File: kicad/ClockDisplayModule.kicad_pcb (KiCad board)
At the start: 2 copper layers, 88.9 x 33 mm, 13 parts, among them P101 CONN_01X05, U101 MAX7221

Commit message: Initial layout before routing
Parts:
- AFF101, AFF102, AFF103, AFF104: value 7SEGMENTS-CC -> NKR161B; footprint ClockFootprints:SC08-11SURKWA -> ClockFootprints:161_163_Series
- U101: footprint SMD_Packages:SOIC-24 -> ClockFootprints:SOIC-24
- moved R101 24.2 mm to (117.9, 39.9), turned to 90 degrees
- moved C101 12.0 mm to (113.8, 40.4), turned to 270 degrees
- moved D104 12.0 mm to (145.8, 41.9)
- moved D103 11.7 mm to (146.1, 61.0)
- moved AFF104 10.9 mm to (93.5, 52.1)
- moved C102 10.9 mm to (115.1, 45.5), turned to 0 degrees
- moved U101 10.4 mm to (115.3, 52.3), turned to 0 degrees
- moved AFF101 9.40 mm to (136.7, 52.1)
- moved P101 9.15 mm to (110.2, 67.1)
- moved AFF103 3.56 mm to (106.4, 52.1)
- moved D101 2.18 mm to (115.6, 47.5)
- moved AFF102 2.03 mm to (123.7, 52.1)
- moved D102 1.63 mm to (115.6, 54.4)
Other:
- net class Default: clearance 0.2 -> 0.254; trace_width 0.25 -> 0.254; via_dia 0.6 -> 0.6858; via_drill 0.4 -> 0.3302
- rule trace_clearance: 0.2 -> 0.254
- rule trace_min: 0.2 -> 0.1524
- rule via_min_drill: 0.3 -> 0.3302
- rule via_min_size: 0.4 -> 0.6858

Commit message: Layout complete and board ordered
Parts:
- added G***: LOGO, ClockFootprints:kicad_logo, F.Cu at (78.7, 65.0)
- added G***: LOGO, ClockFootprints:osh_outline_logo, F.Cu at (77.2, 41.4)
- added R102: 0, Resistors_SMD:R_0805_HandSoldering, F.Cu at (110.0, 47.8)
- added R103: 0, Resistors_SMD:R_0805_HandSoldering, F.Cu at (120.1, 54.6)
- added R104: 0, Resistors_SMD:R_0805_HandSoldering, B.Cu at (150.1, 62.0)
- added R105: 0, Resistors_SMD:R_0805_HandSoldering, B.Cu at (147.3, 38.1)
- moved P101 47.3 mm to (157.5, 66.0), turned to 270 degrees
- moved U101 34.3 mm to (149.6, 52.6), turned to 90 degrees
- moved C102 28.7 mm to (142.2, 54.6), turned to 270 degrees
- moved C101 26.1 mm to (136.4, 53.3), turned to 0 degrees
- moved R101 24.0 mm to (140.0, 49.3), turned to 0 degrees
- moved D101 1.27 mm to (115.6, 48.8)
- moved D102 0.76 mm to (115.6, 53.6), turned to 270 degrees
- turned D103 to 270 degrees
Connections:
- AFF101 pad 5: Net-(AFF101-Pad5) -> (no net)
- AFF102 pad 5: Net-(AFF102-Pad5) -> (no net)
- AFF103 pad 5: Net-(AFF103-Pad5) -> (no net)
- AFF104 pad 5: Net-(AFF104-Pad5) -> (no net)
- D101 pad 1: Signal -> Colon
- D101 pad 2: Seg_A -> Net-(D101-Pad2)
- D102 pad 1: Signal -> Colon
- D102 pad 2: Seg_B -> Net-(D102-Pad2)
- D103 pad 2: Seg_C -> Net-(D103-Pad2)
- D104 pad 2: Seg_D -> Net-(D104-Pad2)
- U101 pad 10: Net-(U101-Pad10) -> Signal
- U101 pad 22: Net-(U101-Pad22) -> (no net)
- U101 pad 24: Net-(U101-Pad24) -> (no net)
- U101 pad 3: Signal -> Colon
- U101 pad 5: Net-(U101-Pad5) -> (no net)
- U101 pad 8: Net-(U101-Pad8) -> (no net)
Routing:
- net Seg_A: track 0.00 -> 112.7 mm, vias 0 -> 7
- net Seg_B: track 0.00 -> 99.9 mm, vias 0 -> 2
- net Seg_G: track 0.00 -> 92.6 mm, vias 0 -> 6
- net Dig_3: track 0.00 -> 91.0 mm, vias 0 -> 1
- net Seg_F: track 0.00 -> 84.0 mm, vias 0 -> 6
- net Dig_2: track 0.00 -> 78.9 mm, vias 0 -> 1
- net Seg_E: track 0.00 -> 74.3 mm, vias 0 -> 4
- net Dig_0: track 0.00 -> 70.5 mm, vias 0 -> 3
- net Seg_C: track 0.00 -> 67.5 mm, vias 0 -> 1
- net Seg_D: track 0.00 -> 64.1 mm, vias 0 -> 4
- net Dig_1: track 0.00 -> 60.7 mm, vias 0 -> 1
- net Colon: track 0.00 -> 59.2 mm, vias 0 -> 1
- net Signal: track 0.00 -> 27.9 mm, vias 0 -> 1
- net CLK: track 0.00 -> 25.1 mm, vias 0 -> 2
- net ~SS: track 0.00 -> 24.5 mm, vias 0 -> 1
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- added copper zone on GND, net GND
- added copper zone on V+, net V+
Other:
- copper layers 2 -> 4
- board text added: "+"
- board text added: "CLK"
- board text added: "Clock Display Module Rev 4L.2"
- board text added: "G"
- board text added: "MOSI"
- board text added: "~SS"

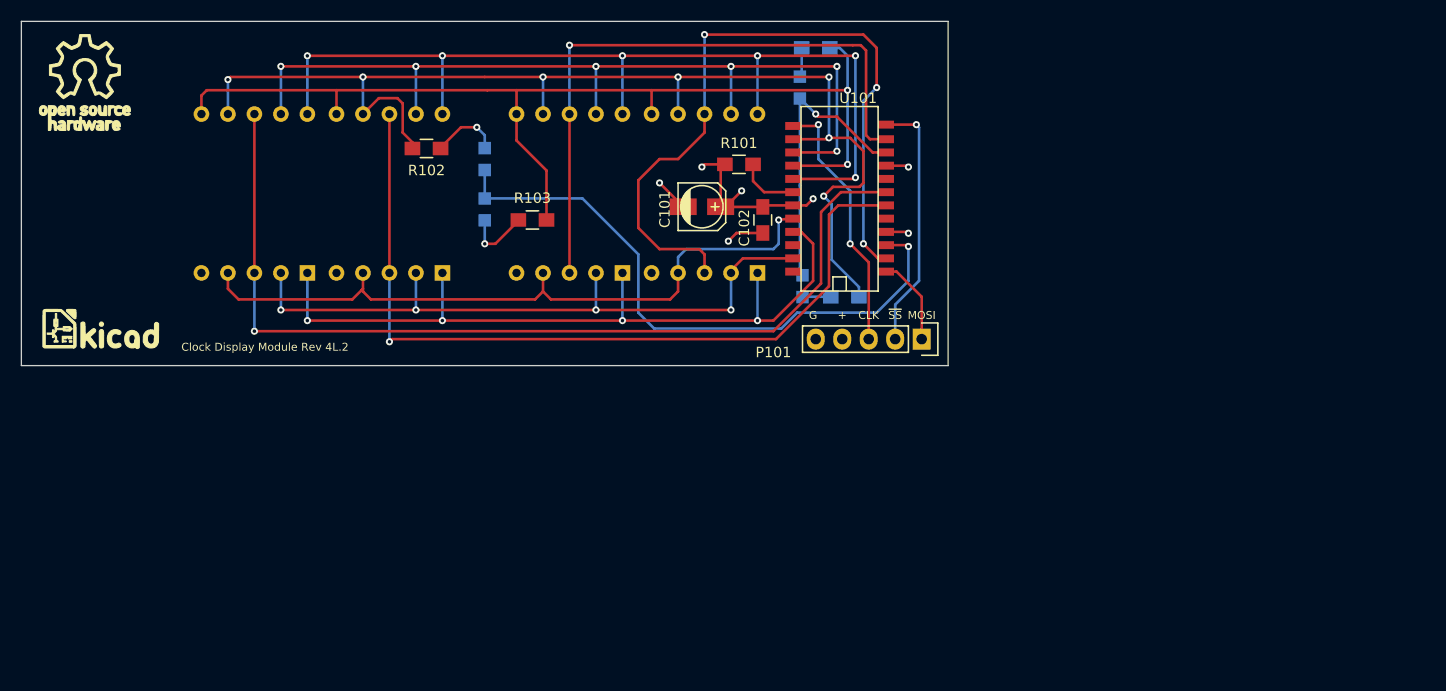
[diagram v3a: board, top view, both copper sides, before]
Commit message: Started layout
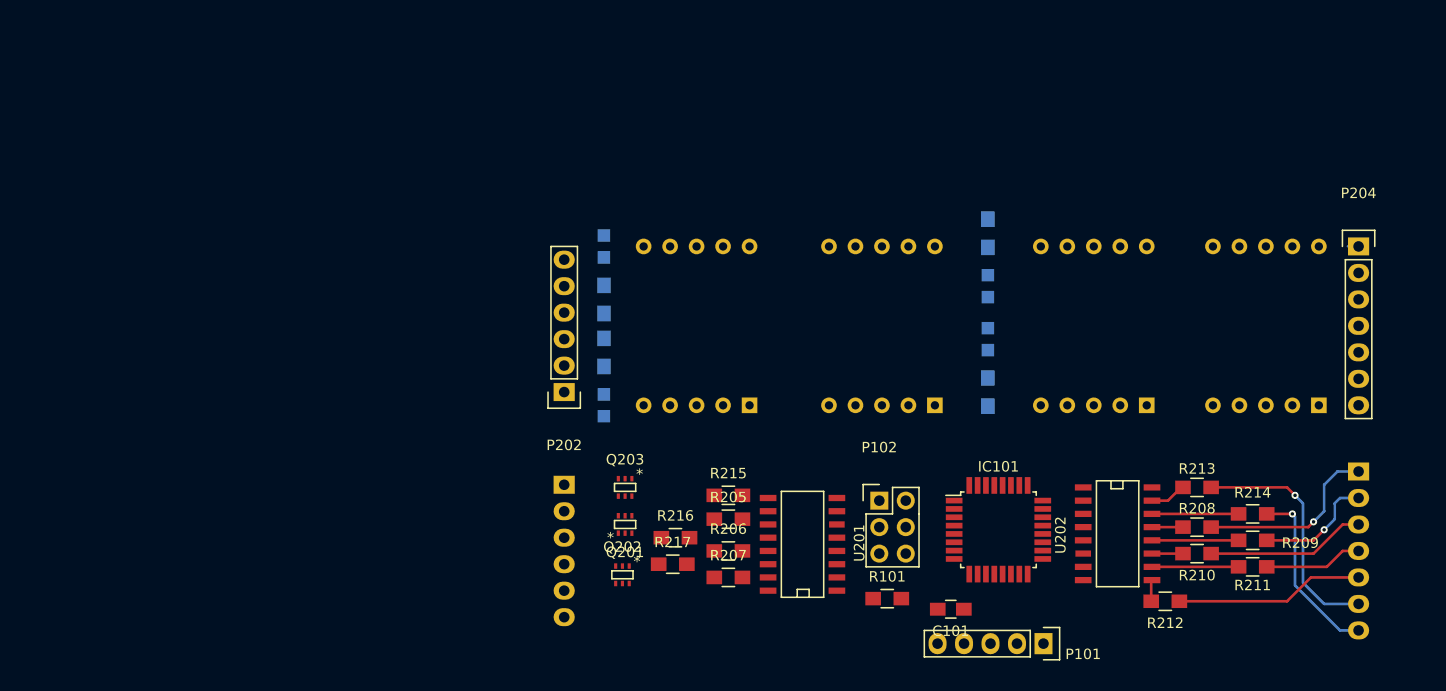
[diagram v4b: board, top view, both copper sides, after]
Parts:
- removed AFF101, AFF102, AFF103, AFF104: NKR161B, ClockFootprints:161_163_Series
- removed C102: 0.1u, Capacitors_SMD:C_0805_HandSoldering
- removed D101: Colon1, LEDs:LED-0805
- removed D102: Colon2, LEDs:LED-0805
- removed D103: Alarm, LEDs:LED-0805
- removed D104: Auto, LEDs:LED-0805
- removed G***: LOGO, ClockFootprints:kicad_logo
- removed G***: LOGO, ClockFootprints:osh_outline_logo
- removed R102, R103, R104, R105: 0, Resistors_SMD:R_0805_HandSoldering
- removed U101: MAX7221, ClockFootprints:SOIC-24
- added AFF201: NKR161B, ClockFootprints:161_163_Series, B.Cu at (135.9, 64.8)
- added AFF202: NKR161B, ClockFootprints:161_163_Series, B.Cu at (174.0, 64.8)
- added AFF203: NKR161B, ClockFootprints:161_163_Series, B.Cu at (153.7, 64.8)
- added AFF204: NKR161B, ClockFootprints:161_163_Series, B.Cu at (190.5, 64.8)
- added D201: Colon1, LEDs:LED-0805, B.Cu at (163.8, 66.0)
- added D202: Colon2, LEDs:LED-0805, B.Cu at (163.8, 61.0)
- added D203: Alarm, LEDs:LED-0805, B.Cu at (127.0, 57.1)
- added D204: Auto, LEDs:LED-0805, B.Cu at (127.0, 72.4)
- added IC101: ATMEGA8-P, Housings_QFP:TQFP-32_7x7mm_Pitch0.8mm, F.Cu at (164.8, 84.3)
- added P102: CONN_02X03, Pin_Headers:Pin_Header_Straight_2x03, F.Cu at (153.4, 81.5)
- added P201: CONN_01X07, Pin_Headers:Pin_Header_Straight_1x07, B.Cu at (199.4, 78.7)
- added P202: CONN_01X06, Pin_Headers:Pin_Header_Straight_1x06, F.Cu at (123.2, 71.1)
- added P203: CONN_01X06, Pin_Headers:Pin_Header_Straight_1x06, B.Cu at (123.2, 80.0)
- added P204: CONN_01X07, Pin_Headers:Pin_Header_Straight_1x07, F.Cu at (199.4, 57.1)
- added Q201: BC856BS, ClockFootprints:SOT-363, F.Cu at (129.0, 83.8)
- added Q202: BC856BS, ClockFootprints:SOT-363, F.Cu at (128.8, 88.6)
- added Q203: BC856BS, ClockFootprints:SOT-363, F.Cu at (129.0, 80.3)
- added R201: 0, Resistors_SMD:R_0805_HandSoldering, B.Cu at (163.8, 71.1)
- added R202: 0, Resistors_SMD:R_0805_HandSoldering, B.Cu at (163.8, 55.9)
- added R203: 0, Resistors_SMD:R_0805_HandSoldering, B.Cu at (127.0, 62.2)
- added R204: 0, Resistors_SMD:R_0805_HandSoldering, B.Cu at (127.0, 67.3)
- added R205: 500, Resistors_SMD:R_0805_HandSoldering, F.Cu at (138.9, 83.3)
- added R206: 500, Resistors_SMD:R_0805_HandSoldering, F.Cu at (138.9, 86.4)
- added R207: 500, Resistors_SMD:R_0805_HandSoldering, F.Cu at (138.9, 88.9)
- added R208: 160, Resistors_SMD:R_0805_HandSoldering, F.Cu at (183.9, 84.1)
- added R209: 160, Resistors_SMD:R_0805_HandSoldering, F.Cu at (189.2, 85.3)
- added R210: 160, Resistors_SMD:R_0805_HandSoldering, F.Cu at (183.9, 86.6)
- added R211: 160, Resistors_SMD:R_0805_HandSoldering, F.Cu at (189.2, 87.9)
- added R212: 160, Resistors_SMD:R_0805_HandSoldering, F.Cu at (180.8, 91.2)
- added R213: 160, Resistors_SMD:R_0805_HandSoldering, F.Cu at (183.9, 80.3)
- added R214: 160, Resistors_SMD:R_0805_HandSoldering, F.Cu at (189.2, 82.8)
- added R215: 500, Resistors_SMD:R_0805_HandSoldering, F.Cu at (138.9, 81.0)
- added R216: 500, Resistors_SMD:R_0805_HandSoldering, F.Cu at (133.9, 85.1)
- added R217: 500, Resistors_SMD:R_0805_HandSoldering, F.Cu at (133.6, 87.6)
- added U201: SN74LS138, ClockFootprints:SOIC-16, F.Cu at (146.1, 85.6)
- added U202: 74HC4511, ClockFootprints:SOIC-16, F.Cu at (176.3, 84.8)
- C101: value 10u -> 0.1u; footprint Capacitors_SMD:c_elec_4x5.8 -> Capacitors_SMD:C_0805_HandSoldering
- R101: value 25K -> 10K
- moved C101 45.4 mm to (160.3, 91.9), turned to 180 degrees
- moved R101 44.0 mm to (154.2, 90.9)
- moved P101 31.5 mm to (169.2, 95.2)
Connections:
- net V+ renamed VCC
- R101 pad 2: Net-(R101-Pad2) -> Reset
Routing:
- net Seg_A: track 112.7 -> 0.00 mm, vias 7 -> 0
- net Seg_B: track 99.9 -> 0.00 mm, vias 2 -> 0
- net Seg_G: track 92.6 -> 0.00 mm, vias 6 -> 0
- net Dig_3: track 91.0 -> 0.00 mm, vias 1 -> 0
- net Seg_F: track 84.0 -> 0.00 mm, vias 6 -> 0
- net Dig_2: track 78.9 -> 0.00 mm, vias 1 -> 0
- net Seg_E: track 74.3 -> 0.00 mm, vias 4 -> 0
- net Dig_0: track 70.5 -> 0.00 mm, vias 3 -> 0
- net Seg_C: track 67.5 -> 0.00 mm, vias 1 -> 0
- net Seg_D: track 64.1 -> 0.00 mm, vias 4 -> 0
- net Dig_1: track 60.7 -> 0.00 mm, vias 1 -> 0
- net Colon: track 59.2 -> 0.00 mm, vias 1 -> 0
- net Signal: track 27.9 -> 0.00 mm, vias 1 -> 0
- net CLK: track 25.1 -> 0.00 mm, vias 2 -> 0
- net ~SS: track 24.5 -> 0.00 mm, vias 1 -> 0
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- removed copper zone on GND, net GND
- removed copper zone on V+, net VCC
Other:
- board outline removed
- copper layers 4 -> 2
- board text removed: "+"
- board text removed: "CLK"
- board text removed: "Clock Display Module Rev 4L.2"
- board text removed: "G"
- board text removed: "MOSI"
- board text removed: "~SS"

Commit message: Updated the layout for the controller side
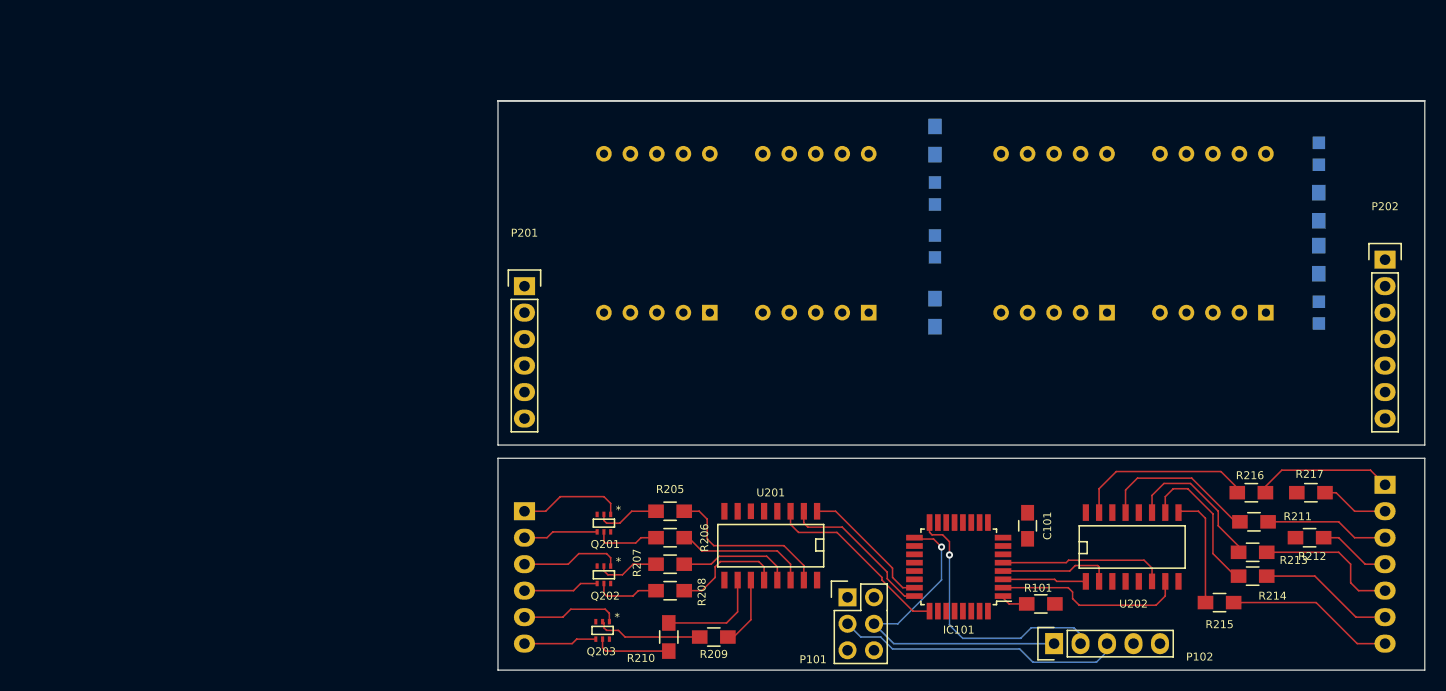
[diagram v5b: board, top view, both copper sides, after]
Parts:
- P101: value CONN_01X05 -> CONN_02X03; footprint Pin_Headers:Pin_Header_Straight_1x05 -> Pin_Headers:Pin_Header_Straight_2x03
- P102: value CONN_02X03 -> CONN_01X05; footprint Pin_Headers:Pin_Header_Straight_2x03 -> Pin_Headers:Pin_Header_Straight_1x05
- P201: value CONN_01X07 -> CONN_01X06; footprint Pin_Headers:Pin_Header_Straight_1x07 -> Pin_Headers:Pin_Header_Straight_1x06; moved to F.Cu
- P202: value CONN_01X06 -> CONN_01X07; footprint Pin_Headers:Pin_Header_Straight_1x06 -> Pin_Headers:Pin_Header_Straight_1x07
- P204: moved to B.Cu
- R208, R209, R210: value 160 -> 500
- R215, R216, R217: value 500 -> 160
- moved P201 82.0 mm to (119.4, 61.0), turned to 0 degrees
- moved P202 79.8 mm to (201.9, 58.4), turned to 0 degrees
- moved D203 69.2 mm to (195.6, 48.3)
- moved D204 69.2 mm to (195.6, 63.5)
- moved R203 69.2 mm to (195.6, 53.3)
- moved R204 69.2 mm to (195.6, 58.4)
- moved R217 61.6 mm to (194.8, 80.8), turned to 180 degrees
- moved AFF204 59.1 mm to (132.1, 55.9)
- moved R216 55.4 mm to (189.1, 80.8), turned to 180 degrees
- moved R209 52.5 mm to (137.5, 94.6), turned to 0 degrees
- moved R210 51.3 mm to (133.2, 94.6), turned to 90 degrees
- moved R208 50.9 mm to (133.3, 90.2), turned to 0 degrees
- moved AFF201 50.3 mm to (185.4, 55.9)
- moved R215 48.2 mm to (186.1, 91.3), turned to 180 degrees
- moved P204 23.0 mm to (201.9, 80.0), turned to 180 degrees
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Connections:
- AFF201 pad 5: Net-(AFF201-Pad5) -> (no net)
- AFF202 pad 5: Net-(AFF202-Pad5) -> (no net)
- AFF203 pad 5: Net-(AFF203-Pad5) -> (no net)
- AFF204 pad 5: Net-(AFF204-Pad5) -> (no net)
- IC101 pad 10: Net-(IC101-Pad10) -> (no net)
- IC101 pad 11: Net-(IC101-Pad11) -> (no net)
- IC101 pad 12: Net-(IC101-Pad12) -> (no net)
- IC101 pad 13: Net-(IC101-Pad13) -> (no net)
- IC101 pad 14: Net-(IC101-Pad14) -> (no net)
- IC101 pad 15: Net-(IC101-Pad15) -> (no net)
- IC101 pad 18: Net-(IC101-Pad18) -> MISO
- IC101 pad 21: Net-(IC101-Pad21) -> (no net)
- IC101 pad 26: Net-(IC101-Pad26) -> (no net)
- IC101 pad 27: Net-(IC101-Pad27) -> (no net)
- IC101 pad 28: Net-(IC101-Pad28) -> (no net)
- IC101 pad 6: Net-(IC101-Pad6) -> (no net)
- IC101 pad 9: Net-(IC101-Pad9) -> (no net)
- P101 pad 1: MOSI -> MISO
- P101 pad 2: ~SS -> VCC
- P101 pad 4: VCC -> MOSI
- P101 pad 5: GND -> Reset
- P102 pad 2: VCC -> ~SS
- P102 pad 4: MOSI -> VCC
- P102 pad 5: Reset -> GND
- P201 pad 1: Net-(P201-Pad1) -> D_Dig_0
- P201 pad 2: Net-(P201-Pad2) -> D_Dig_1
- P201 pad 3: Net-(P201-Pad3) -> D_Dig_2
- P201 pad 4: Net-(P201-Pad4) -> D_Dig_3
- P201 pad 5: Net-(P201-Pad5) -> D_Colon
- P201 pad 6: Net-(P201-Pad6) -> D_Signal
- P202 pad 1: D_Dig_0 -> /Display Driver/Seg_A
- P202 pad 2: D_Dig_1 -> /Display Driver/Seg_B
- P202 pad 3: D_Dig_2 -> /Display Driver/Seg_C
- P202 pad 4: D_Dig_3 -> /Display Driver/Seg_D
- P202 pad 5: D_Colon -> /Display Driver/Seg_E
- P202 pad 6: D_Signal -> /Display Driver/Seg_F
- P204 pad 1: /Display Driver/Seg_A -> /Display Driver/C_Seg_F
- P204 pad 2: /Display Driver/Seg_B -> /Display Driver/C_Seg_G
- P204 pad 3: /Display Driver/Seg_C -> /Display Driver/C_Seg_A
- P204 pad 4: /Display Driver/Seg_D -> /Display Driver/C_Seg_B
- P204 pad 5: /Display Driver/Seg_E -> /Display Driver/C_Seg_C
- P204 pad 6: /Display Driver/Seg_F -> /Display Driver/C_Seg_D
- P204 pad 7: /Display Driver/Seg_G -> /Display Driver/C_Seg_E
- Q201 pad 1: C_Colon -> C_Dig_0
- Q201 pad 4: C_Dig_2 -> C_Dig_1
- Q202 pad 1: C_Dig_0 -> C_Dig_2
- Q203 pad 1: C_Dig_1 -> C_Colon
- R208 pad 1: Net-(P201-Pad1) -> Net-(Q202-Pad5)
- R209 pad 1: Net-(P201-Pad2) -> Net-(Q203-Pad2)
- R210 pad 1: Net-(P201-Pad3) -> Net-(Q203-Pad5)
- R211 pad 1: Net-(P201-Pad4) -> /Display Driver/C_Seg_A
- R212 pad 1: Net-(P201-Pad5) -> /Display Driver/C_Seg_B
- R213 pad 1: Net-(P201-Pad6) -> /Display Driver/C_Seg_C
- R214 pad 1: Net-(P201-Pad7) -> /Display Driver/C_Seg_D
- R215 pad 1: Net-(Q203-Pad5) -> /Display Driver/C_Seg_E
- R216 pad 1: Net-(Q202-Pad5) -> /Display Driver/C_Seg_F
- R217 pad 1: Net-(Q203-Pad2) -> /Display Driver/C_Seg_G
- U201 pad 10: Net-(R215-Pad2) -> Net-(R210-Pad2)
- U201 pad 11: Net-(R205-Pad2) -> Net-(R209-Pad2)
- U201 pad 12: Net-(R216-Pad2) -> Net-(R208-Pad2)
- U201 pad 13: Net-(R206-Pad2) -> Net-(R207-Pad2)
- U201 pad 14: Net-(R217-Pad2) -> Net-(R206-Pad2)
- U201 pad 15: Net-(R207-Pad2) -> Net-(R205-Pad2)
- U201 pad 7: Net-(U201-Pad7) -> (no net)
- U201 pad 9: Net-(U201-Pad9) -> (no net)
- U202 pad 10: Net-(R211-Pad2) -> Net-(R214-Pad2)
- U202 pad 11: Net-(R210-Pad2) -> Net-(R213-Pad2)
- U202 pad 12: Net-(R209-Pad2) -> Net-(R212-Pad2)
- U202 pad 13: Net-(R208-Pad2) -> Net-(R211-Pad2)
- U202 pad 14: Net-(R214-Pad2) -> Net-(R217-Pad2)
- U202 pad 15: Net-(R213-Pad2) -> Net-(R216-Pad2)
- U202 pad 9: Net-(R212-Pad2) -> Net-(R215-Pad2)
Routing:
- net MOSI: track 0.00 -> 32.4 mm, vias 0 -> 1
- net CLK: track 0.00 -> 27.6 mm
- net ~SS: track 0.00 -> 26.0 mm, vias 0 -> 1
- net Net-(P201-Pad6): track 23.2 -> 0.00 mm, vias 1 -> 0
- net A: track 0.00 -> 18.4 mm
- net A2: track 0.00 -> 18.2 mm
- net Net-(P201-Pad5): track 18.1 -> 0.00 mm
- net Net-(P201-Pad1): track 17.8 -> 0.00 mm, vias 1 -> 0
- net Net-(P201-Pad7): track 17.7 -> 0.00 mm, vias 1 -> 0
- net Net-(R216-Pad2): track 0.00 -> 17.3 mm
- net Net-(R205-Pad2): track 0.00 -> 16.8 mm
- net /Display Driver/C_Seg_E: track 0.00 -> 16.2 mm
- net D: track 0.00 -> 16.0 mm
- net Net-(P201-Pad3): track 15.3 -> 0.00 mm
- net A1: track 0.00 -> 15.0 mm
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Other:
- board outline added: 88.9 x 54.6 mm
- net class Default: trace_width 0.254 -> 0.1524
